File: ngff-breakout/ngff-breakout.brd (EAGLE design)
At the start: 70 x 70 mm, 43 parts, among them K1 694108106102, U1 IP4234CZ6, U2 LD1085D2T33R, X2 MINI-USB-SHIELD-UX60-MB-5ST

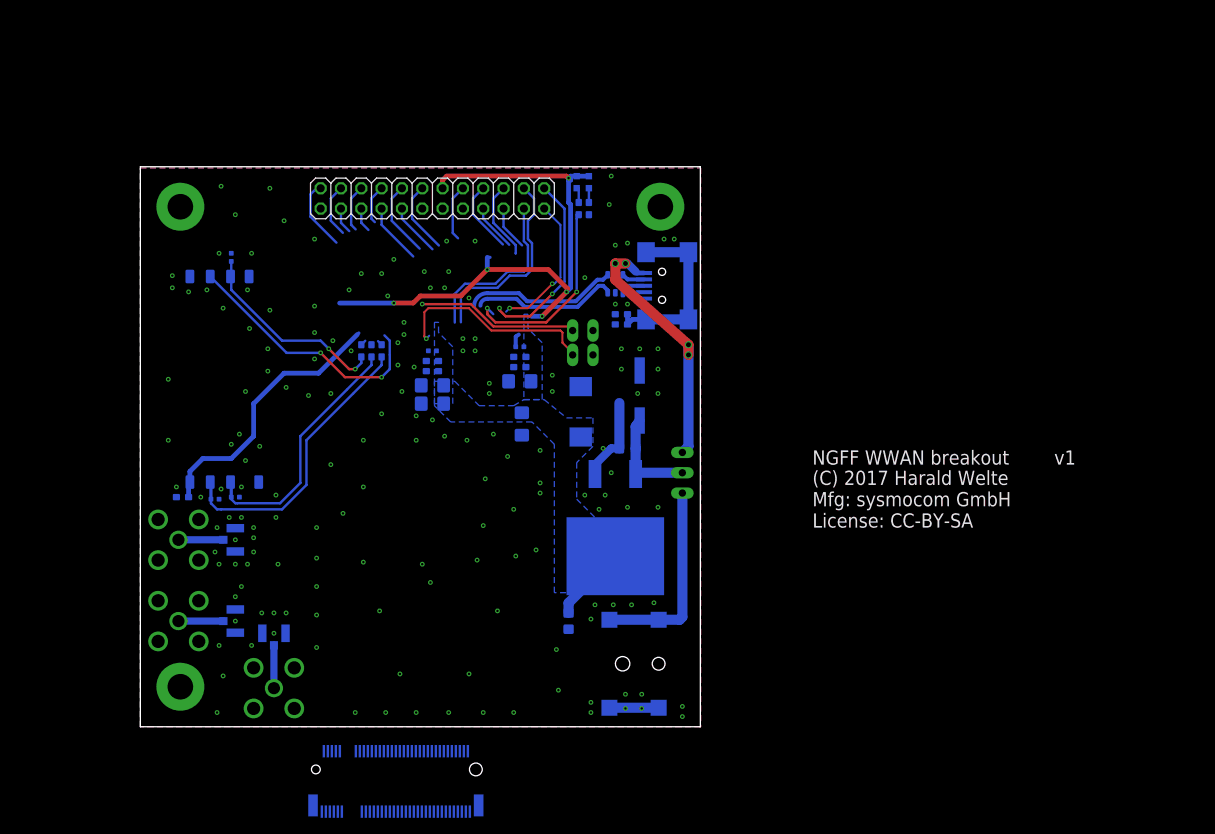
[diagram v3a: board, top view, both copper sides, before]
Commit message: ngff-breakout: intermediate state
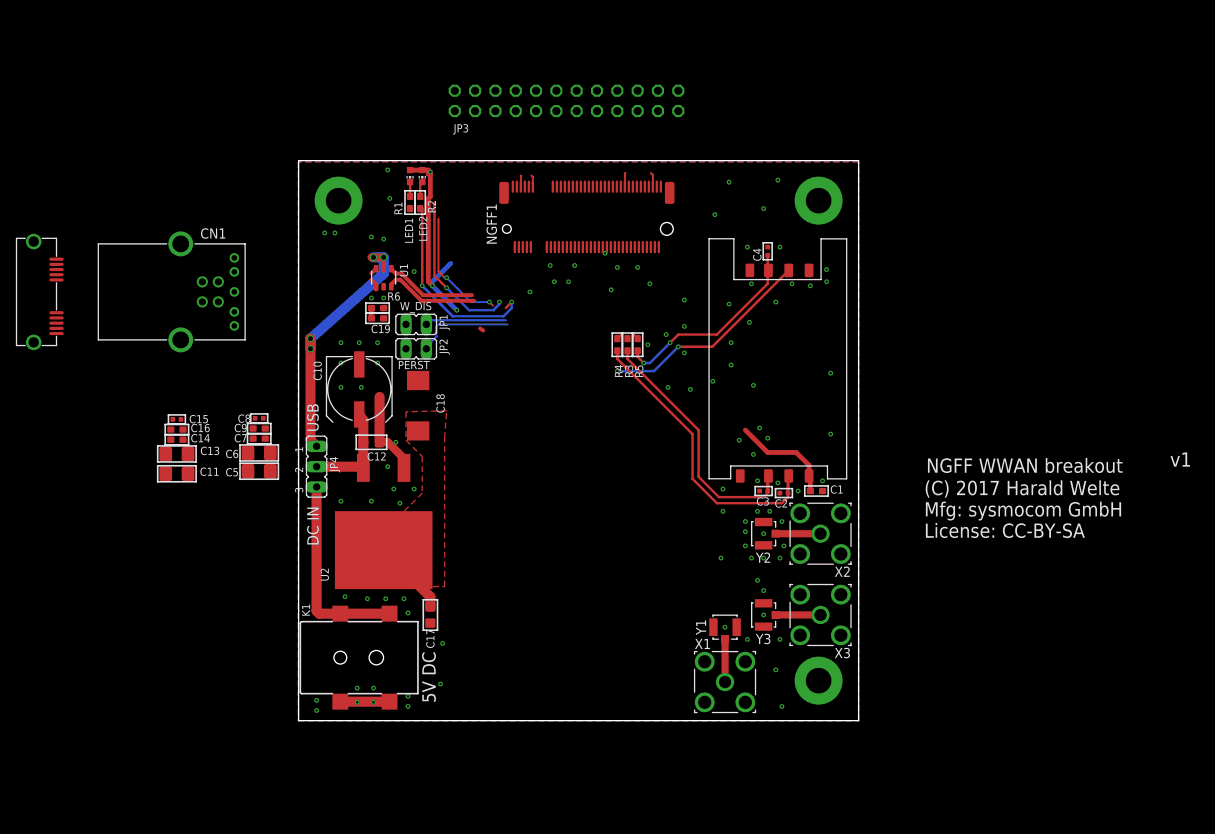
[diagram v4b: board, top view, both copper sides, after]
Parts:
- removed C105, C109: 100u, rc-sysmocom:1206
- removed C106, C110: 100n, rc-sysmocom:_0603
- removed C107, C111: 33p, rc-sysmocom:_0402
- removed C108, C112: 10p, rc-sysmocom:_0603
- removed X4, X5: (no value), laforge:SMA-F-S-TH
- removed Y4, Y5: (no value), laforge:HRS_UFL
- added C12, C17: 10u, rc-sysmocom:_0805
- added C13: 100u, rc-sysmocom:1206
- added C14, C19: 100n, rc-sysmocom:_0603
- added C15: 33p, rc-sysmocom:_0402
- added C16: 10p, rc-sysmocom:_0603
- added C18: DNP, rcl:SMC_E
- added CN1: (no value), USB30B:USB3.0-B
- added CN2: (no value), USB30-MICROB:ZX360D-B
- added X1: (no value), laforge:SMA-F-S-TH
- added Y1, Y2: (no value), laforge:HRS_UFL
- C1: value 10u -> 100n; device rc-sysmocom:_0805 -> rc-sysmocom:_0603
- C10: value 100u -> 470u; device rc-sysmocom:1206 -> rcl:UD-8X10_NICHICON
- C2: value 10u -> 33p; device rc-sysmocom:_0805 -> rc-sysmocom:_0402
- C3: value 470u -> 33p; device rcl:UD-8X10_NICHICON -> rc-sysmocom:_0402
- C4: value DNP -> 33p; device rcl:SMC_E -> rc-sysmocom:_0402
- C5, C6: value 33p -> 100u; device rc-sysmocom:_0402 -> rc-sysmocom:1206
- C7: value 33p -> 100n; device rc-sysmocom:_0402 -> rc-sysmocom:_0603
- C8: value 100n -> 33p; device rc-sysmocom:_0603 -> rc-sysmocom:_0402
- C9: value 100n -> 10p
- JP3: device jumper:JP2 -> pinhead:2X12
- JP4: device pinhead:2X12 -> jumper:JP2
- LED1: value YELLOW -> GREEN
- LED2: value GREEN -> YELLOW
- R1, R2: value 47 -> 330
- R4: value 1M -> 47
- R5: value 330 -> 47
- R6: value 330 -> 1M
- X2: value MINI-USB-SHIELD-UX60-MB-5ST -> (none); device con-hirose:UX60-MB-5ST -> laforge:SMA-F-S-TH
- moved X3 80.8 mm to (65.0, 14.0), flipped to the top
- moved NGFF1 71.7 mm to (35.8, 62.2), flipped to the top, turned to 0 degrees
- moved SIM1 69.6 mm to (59.7, 44.2), flipped to the top
- moved Y3 66.7 mm to (57.9, 14.0), flipped to the top
- moved K1 49.8 mm to (0.00, 8.64), flipped to the top
- moved JP3 48.7 mm to (33.3, 78.2), turned to 0 degrees
- moved C9 47.1 mm to (-5.14, 37.3), flipped to the top, turned to 0 degrees
- moved C11 43.6 mm to (-15.4, 31.6), flipped to the top, turned to 180 degrees
- moved X2 36.8 mm to (65.0, 24.1), flipped to the top, turned to 180 degrees
- moved JP4 36.5 mm to (2.03, 32.5), turned to 270 degrees
- moved C2 31.3 mm to (60.5, 29.2), flipped to the top, turned to 180 degrees
- moved C4 30.8 mm to (58.4, 59.4), flipped to the top
- moved R3 30.7 mm to (40.9, 47.8), flipped to the top
- moved U1 29.0 mm to (10.4, 56.1), flipped to the top
- moved U2 29.0 mm to (10.4, 25.7), flipped to the top
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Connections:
- removed net N$14 (its old number): X4.C, Y4.SIG
- new net N$11: CN1.6
- new net N$13: X2.C, Y2.SIG
- new net N$15: CN1.7
- new net N$17: CN1.8
- new net N$18: CN1.9
- new net N$4: CN1.5
- new net USB3.0_RX_N: NGFF1.35
- new net USB3.0_RX_P: NGFF1.37
- new net USB3.0_TX_N: NGFF1.29
- new net USB3.0_TX_P: NGFF1.31
- net !CLKREQ: now also JP3.6; no longer JP4.6
- net COEX1: now also JP3.4; no longer JP4.4
- net COEX2: now also JP3.3; no longer JP4.3
- net GND: now also C10.-, C12.1, C13.1, C14.1, C15.2, C16.2, C17.1, C18.-, C19.1, C2.2, C3.2, C4.2, C5.1, C6.1, C7.1, C8.2, C9.2, CN1.4, JP1.1, JP2.2, JP3.1, JP3.13, R1.1, R6.1, X1.G1, X1.G2, X1.G3, X1.G4, X2.G1, X2.G2, X2.G3, X2.G4, Y1.GND@1, Y1.GND@2, Y2.GND@1, Y2.GND@2; no longer C10.1, C105.1, C106.1, C107.2, C108.2, C109.1, C110.1, C111.2, C112.2, C2.1, C3.-, C4.-, C5.2, C6.2, C7.2, C8.1, C9.1, JP1.2, JP2.1, JP4.1, JP4.13, R4.1, R5.1, X2.5, X4.G1, X4.G2, X4.G3, X4.G4, X5.G1, X5.G2, X5.G3, X5.G4, Y4.GND@1, Y4.GND@2, Y5.GND@1, Y5.GND@2
- net LDO_IN: now also C10.+, C12.2, JP4.2; no longer C1.2, C3.+, JP3.2
- net LED_WLAN: now also JP3.24; no longer JP4.24
- net LED_WPAN: now also JP3.23; no longer JP4.23
- net N$1: now also LED1.C, R1.2; no longer LED2.C, R5.2
- net N$10: now also C19.2, CN1.S1, CN1.S2, R6.2; no longer C9.2, R4.2, X2.M1, X2.M2, X2.M3, X2.M4
- net N$12: now also JP4.3; no longer JP3.3
- net N$16: now also JP3.11; no longer JP4.11
- net N$2: now also LED2.C, R2.1; no longer LED1.C, R6.1
- net N$3: now also R2.2; no longer R6.2
- net N$5: now also R5.1; no longer R1.1
- net N$7: now also X1.C, Y1.SIG; no longer X5.C, Y5.SIG
- net N$8: now also R3.1; no longer R2.1
- net N$9: now also R4.1; no longer R3.1
- net PERN0: now also JP3.9; no longer JP4.9
- net PERP0: now also JP3.12; no longer JP4.12
- net PERST: now also JP2.1; no longer JP1.1
- net PETN0: now also JP3.16; no longer JP4.16
- net PETP0: now also JP3.15; no longer JP4.15
- net REFCLK+: now also JP3.8; no longer JP4.8
- net REFCLK-: now also JP3.5; no longer JP4.5
- net RSVRD45: now also JP3.18; no longer JP4.18
- net RSVRD47: now also JP3.17; no longer JP4.17
- net RSVRD49: now also JP3.20; no longer JP4.20
- net RSVRD51: now also JP3.19; no longer JP4.19
- net SMB_CLK: now also JP3.21; no longer JP4.21
- net SMB_DATA: now also JP3.22; no longer JP4.22
- net UIM_C4: now also JP3.10; no longer JP4.10
- net UIM_C8: now also JP3.7; no longer JP4.7
- net USB_VBUS: now also CN1.1, JP4.1; no longer JP3.1, X2.1
- net USIM_CLK: now also C3.1, R3.2; no longer C5.1, R2.2
- net USIM_DATA: now also C4.1, R5.2; no longer C7.1, R1.2
- net USIM_POWER: now also C1.2; no longer C8.2
- net USIM_RESET: now also C2.1, R4.2; no longer C6.1, R3.2
- net VCC_3V3: now also C13.2, C14.2, C15.1, C16.1, C17.2, C18.+, C5.2, C6.2, C7.2, C8.1, C9.1, JP3.14; no longer C10.2, C105.2, C106.2, C107.1, C108.1, C109.2, C110.2, C111.1, C112.1, C2.2, C4.+, JP4.14
- net WAKE: now also JP3.2; no longer JP4.2
- net W_DISABLE: now also JP1.2; no longer JP2.2
- net _USB_D_N: now also CN1.2; no longer X2.2
- net _USB_D_P: now also CN1.3; no longer X2.3
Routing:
- net VCC_3V3: track 83.3 -> 35.2 mm, vias 5 -> 3
- net SMB_DATA: track 24.9 -> 0.00 mm
- net SMB_CLK: track 21.7 -> 0.00 mm
- net N$10: track 22.8 -> 1.27 mm
- net USIM_POWER: track 33.9 -> 13.1 mm
- net PERST: track 26.0 -> 12.3 mm, vias 1 -> 0
- net W_DISABLE: track 20.3 -> 10.1 mm, vias 1 -> 0
- net RSVRD49: track 9.83 -> 0.00 mm
- net UIM_C4: track 9.51 -> 0.00 mm
- net RSVRD45: track 9.09 -> 0.00 mm
- net PERP0: track 9.06 -> 0.00 mm
- net WAKE: track 8.96 -> 0.00 mm
- net USB_D_N: track 19.2 -> 11.5 mm
- net UIM_C8: track 7.62 -> 0.00 mm
- net PETN0: track 7.05 -> 0.00 mm
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- added copper zone on layer 1, net VCC_3V3
- removed copper zone on layer 16, net VCC_3V3
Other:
- board text removed: "1"

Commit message: ngff-breakout: almost ready
missing: more vias, more ext. attributes (for BOM)
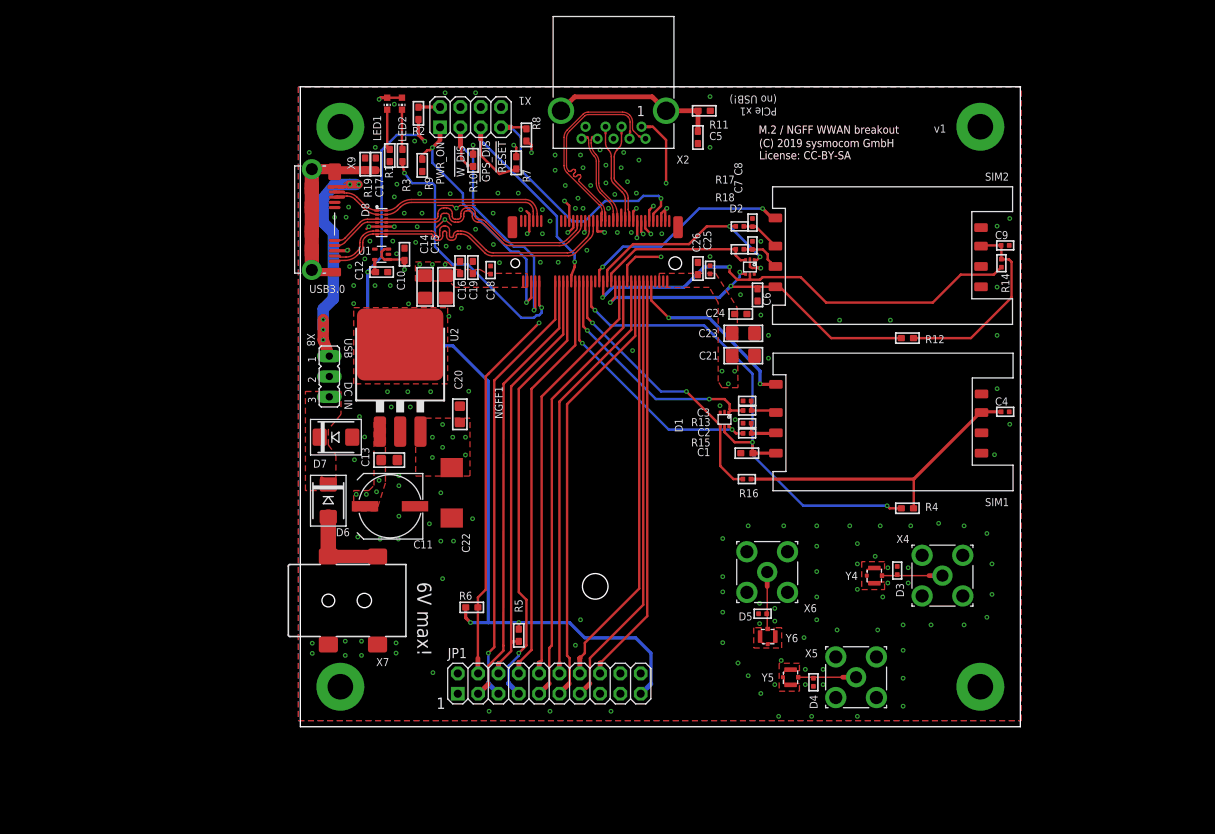
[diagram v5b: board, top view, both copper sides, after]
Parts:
- removed CN1: (no value), USB30B:USB3.0-B
- removed CN2: (no value), USB30-MICROB:ZX360D-B
- removed JP2: (no value), jumper:JP1
- removed JP3: (no value), pinhead:2X12
- removed JP4: (no value), jumper:JP2
- removed K1: 694108106102, Wurth_Elektronik_Electromechanic_DC_Power_Jack_Connectors_rev15c:694108106102
- removed X3: (no value), laforge:SMA-F-S-TH
- removed Y1, Y2, Y3: (no value), laforge:HRS_UFL
- added C20: 10u, rc-sysmocom:_0805
- added C21, C23: 100u, rc-sysmocom:1206
- added C22: DNP, rcl:SMC_E
- added C24: 100n, rc-sysmocom:_0603
- added C25: 33p, rc-sysmocom:_0402
- added C26: 10p, rc-sysmocom:_0603
- added D1, D2: PESD5V0UBV, laforge:SOT666
- added D3, D4, D5: GG040205170N2P, diodes-sysmocom:_0402
- added D6: SD2114S040S5R0, diodes-sysmocom:SMBDIODE
- added D7: SMBJP6KE6.8A-TP, diodes-sysmocom:SMBDIODE
- added D8: SP3012-6UTG, SP3012:UDFN-14
- added R10, R7, R8, R9: 10k, rc-sysmocom:_0603
- added R11, R19: 330, rc-sysmocom:_0603
- added R12: DNP, rc-sysmocom:_0603
- added R13, R14, R15, R16, R17, R18: 47, rc-sysmocom:_0402
- added SIM2: SF7W008S1A-R, SF7W008S1A-SIM:SF7W008S1A-RESTR
- added X4, X5, X6: (no value), laforge:SMA-F-S-TH
- added X7: 694108106102, Wurth_Elektronik_Electromechanic_DC_Power_Jack_Connectors_rev15c:694108106102
- added X8: (no value), jumper:JP2
- added X9: ZX360D-B-10P(30), USB30-MICROB:ZX360D-B
- added Y4, Y5, Y6: MHF4, con-MHF4:MURATA_HSC
- C10: value 470u -> 100n; device rcl:UD-8X10_NICHICON -> rc-sysmocom:_0603
- C11: value 100u -> 470u; device rc-sysmocom:1206 -> rcl:UD-8X10_NICHICON
- C12, C17: value 10u -> 100n; device rc-sysmocom:_0805 -> rc-sysmocom:_0603
- C13: value 100u -> 10u; device rc-sysmocom:1206 -> rc-sysmocom:_0805
- C14: value 100n -> 100u; device rc-sysmocom:_0603 -> rc-sysmocom:1206
- C15: value 33p -> 100u; device rc-sysmocom:_0402 -> rc-sysmocom:1206
- C16: value 10p -> 100n
- C18: value DNP -> 33p; device rcl:SMC_E -> rc-sysmocom:_0402
- C19: value 100n -> 10p
- C5, C6: value 100u -> 100n; device rc-sysmocom:1206 -> rc-sysmocom:_0603
- C7: value 100n -> 33p; device rc-sysmocom:_0603 -> rc-sysmocom:_0402
- C9: value 10p -> 33p; device rc-sysmocom:_0603 -> rc-sysmocom:_0402
- JP1: device jumper:JP1 -> laforge:2X10
- R2: value 330 -> 10k
- R3: value 47 -> 330
- R4: value 47 -> DNP
- R5: value 47 -> 10k
- R6: value 1M -> 10k
- U1: value IP4234CZ6 -> (none); device laforge:TSOP-6 -> ldo:SC70-5
- U2: device ldo:ST_D2PAK -> ldo:TO263
- X1: value (none) -> PINHD-2X4; device laforge:SMA-F-S-TH -> laforge:2X04
- X2: device laforge:SMA-F-S-TH -> InputOutputIO (rev19a):692121030100
- moved C9 96.0 mm to (88.1, 60.2)
- moved X1 77.4 mm to (21.3, 76.2)
- moved C5 68.9 mm to (49.7, 73.7), turned to 90 degrees
- moved C8 66.3 mm to (56.5, 63.0), turned to 90 degrees
- moved C7 66.2 mm to (56.5, 60.2), turned to 90 degrees
- moved C6 65.3 mm to (57.1, 54.0), turned to 90 degrees
- moved C17 56.8 mm to (9.43, 70.3), turned to 270 degrees
- moved X2 55.7 mm to (39.1, 73.5)
- moved JP1 47.9 mm to (31.1, 5.40), turned to 0 degrees
- moved R4 41.6 mm to (75.9, 27.3), turned to 0 degrees
- moved C16 40.8 mm to (20.0, 57.4), turned to 270 degrees
- moved R5 39.2 mm to (27.3, 11.4), turned to 90 degrees
- moved R6 39.2 mm to (21.4, 14.9)
- moved C15 37.5 mm to (18.2, 55.0), turned to 90 degrees
- moved R3 36.8 mm to (12.8, 71.4)
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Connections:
- net USIM_VPP renamed N$8
- removed net LED_WLAN: JP3.24
- removed net LED_WPAN: JP3.23
- removed net N$11: CN1.6
- removed net N$15: CN1.7
- removed net N$16: JP3.11
- removed net N$8 (its old number): NGFF1.32, R3.1
- removed net N$9: NGFF1.30, R4.1
- removed net PERN0: JP3.9
- removed net PERP0: JP3.12
- removed net PERST: JP2.1, NGFF1.67
- removed net PETN0: JP3.16
- removed net PETP0: JP3.15
- removed net REFCLK+: JP3.8
- removed net REFCLK-: JP3.5
- removed net RSVRD45: JP3.18
- removed net RSVRD47: JP3.17
- removed net RSVRD49: JP3.20
- removed net RSVRD51: JP3.19
- removed net UIM_C4: JP3.10
- removed net UIM_C8: JP3.7
- removed net USB_D_N: NGFF1.9, U1.4
- removed net USB_D_P: NGFF1.7, U1.3
- removed net USIM_CLK: C3.1, R3.2, SIM1.3
- removed net USIM_DATA: C4.1, R5.2, SIM1.7
- removed net USIM_POWER: C1.2, NGFF1.36, SIM1.1
- removed net USIM_RESET: C2.1, R4.2, SIM1.2
- removed net WAKE: JP3.2, NGFF1.23
- removed net W_DISABLE: JP1.2, NGFF1.8
- new net !BODY_SAR: JP1.4, NGFF1.25, R6.1
- new net !GPS_DISABLE: NGFF1.26, R7.1, X1.5
- new net !PERST: JP1.10, NGFF1.50
- new net !RESET: NGFF1.67, R8.1, X1.7
- new net !USIM1_RESET: C2.1, R15.2, SIM1.2
- new net !USIM2_RESET: C7.1, R18.2, SIM2.2
- new net !WAKE: NGFF1.54, X2.1
- new net !WAKE_ON_WWAN: JP1.6, NGFF1.23, R5.1
- new net !W_DISABLE: NGFF1.8, R10.1, X1.3
- new net ANTCTL0: JP1.15, NGFF1.59
- new net ANTCTL1: JP1.18, NGFF1.61
- new net ANTCTL2: JP1.17, NGFF1.63
- new net ANTCTL3: JP1.20, NGFF1.65
- new net COEX3: JP1.14, NGFF1.60
- new net N$6: NGFF1.10, R3.2
- new net PCIE_RX_N: NGFF1.47, X2.5
- new net PCIE_RX_P: NGFF1.49, X2.6
- new net PCIE_TX_N: NGFF1.41, X2.9
- new net PCIE_TX_P: NGFF1.43, X2.8
- new net PCM_CLK: JP1.5, NGFF1.20
- new net PCM_DIN: JP1.3, NGFF1.22
- new net PCM_DOUT: JP1.7, NGFF1.24
- new net PCM_SYNC: JP1.8, NGFF1.28
- new net PWR_ON: NGFF1.6, R9.2, X1.1
- new net REFCLK_N: NGFF1.53, X2.3
- new net REFCLK_P: NGFF1.55, X2.2
- new net SIM1_DET: NGFF1.66, SIM1.81
- new net SIM2_DET: NGFF1.40, SIM2.81
- new net USIM1_CLK: C3.1, R13.2, SIM1.3
- new net USIM1_DATA: C4.1, R16.2, R4.2, SIM1.7
- new net USIM1_POWER: C1.2, D1.5, NGFF1.36, R4.1, SIM1.1
- new net USIM2_CLK: C8.1, R17.2, SIM2.3
- new net USIM2_DATA: C9.1, R12.2, R14.2, SIM2.7
- new net USIM2_POWER: C6.2, D2.4, NGFF1.48, R12.1, SIM2.1
- new net VCC_1V8: C12.2, JP1.19, R10.2, R2.2, R5.2, R6.2, R7.2, R8.2, U1.5
- new net _!USIM1_RESET: D1.6, NGFF1.30, R15.1
- new net _!USIM2_RESET: D2.3, NGFF1.46, R18.1
- new net _USIM1_CLK: D1.1, NGFF1.32, R13.1
- new net _USIM1_DATA: D1.4, NGFF1.34, R16.1
- new net _USIM2_CLK: D2.1, NGFF1.44, R17.1
- new net _USIM2_DATA: D2.5, NGFF1.42, R14.1
- net !CLKREQ: now also JP1.9, NGFF1.52; no longer JP3.6
- net COEX1: now also JP1.16; no longer JP3.4
- net COEX2: now also JP1.13; no longer JP3.3
- net GND: now also C10.1, C11.-, C15.1, C16.1, C18.2, C19.2, C20.1, C21.1, C22.-, C23.1, C24.1, C25.2, C26.2, C7.2, D1.2, D2.2, D3.1, D4.1, D5.1, D7.A, D8.10, JP1.2, R11.1, R19.1, R9.1, SIM1.82, SIM2.5, SIM2.82, U2.2, U2.4, X1.4, X1.6, X1.8, X4.G1, X4.G2, X4.G3, X4.G4, X5.G1, X5.G2, X5.G3, X5.G4, X6.G1, X6.G2, X6.G3, X6.G4, X7.2, X7.3, X9.5, X9.8, Y4.P$1, Y4.P$2, Y4.P$4, Y5.P$1, Y5.P$2, Y5.P$4, Y6.P$1, Y6.P$2, Y6.P$4; no longer C10.-, C11.1, C15.2, C16.2, C18.-, C19.1, C7.1, CN1.4, JP1.1, JP2.2, JP3.1, JP3.13, K1.2, K1.3, R6.1, U2.LEFT, X1.G1, X1.G2, X1.G3, X1.G4, X2.G1, X2.G2, X2.G3, X2.G4, X3.G1, X3.G2, X3.G3, X3.G4, Y1.GND@1, Y1.GND@2, Y2.GND@1, Y2.GND@2, Y3.GND@1, Y3.GND@2
- net LDO_IN: now also C11.+, C13.2, U2.1, X8.2; no longer C10.+, C12.2, JP4.2, U2.RIGHT
- net N$10: now also C17.2, R19.2, X9.S1, X9.S2, X9.S3, X9.S4, X9.S5, X9.S6, X9.S7, X9.S8; no longer C19.2, CN1.S1, CN1.S2, R6.2
- net N$12: now also D6.C, D7.C, X8.3; no longer JP4.3, K1.1, K1.1-1
- net N$13: now also D3.2, X4.C, Y4.1; no longer X2.C, Y2.SIG
- net N$14: now also D4.2, X5.C, Y5.1; no longer X3.C, Y3.SIG
- net N$17: now also X9.4; no longer CN1.8
- net N$18: now also R2.1, X1.2; no longer CN1.9
- net N$2: now also R3.1; no longer R2.1
- net N$3: now also D6.A, X7.1, X7.1-1; no longer R2.2
- net N$4: now also C5.2, R11.2, X2.SHELL, X2.SHELL1; no longer CN1.5
- net N$5: now also SIM2.6; no longer NGFF1.34, R5.1
- net N$7: now also D5.2, X6.C, Y6.1; no longer X1.C, Y1.SIG
- net SMB_CLK: now also JP1.11; no longer JP3.21
- net SMB_DATA: now also JP1.12; no longer JP3.22
- net USB3.0_RX_N: now also D8.9, X9.9
- net USB3.0_RX_P: now also D8.8, X9.10
- net USB3.0_TX_N: now also D8.12, X9.6
- net USB3.0_TX_P: now also D8.11, X9.7
- net USB_VBUS: now also X8.1, X9.1; no longer CN1.1, JP4.1, U1.5
- net VCC_3V3: now also C10.2, C15.2, C16.2, C18.1, C19.1, C20.2, C21.2, C22.+, C23.2, C24.2, C25.1, C26.1, JP1.1, U1.1, U1.3, U2.3; no longer C11.2, C13.2, C15.1, C16.1, C17.2, C18.+, C5.2, C6.2, C7.2, C8.1, C9.1, JP3.14, U2.PAD
- net _USB_D_N: now also D8.14, NGFF1.9, X9.2; no longer CN1.2, U1.6
- net _USB_D_P: now also D8.13, NGFF1.7, X9.3; no longer CN1.3, U1.1
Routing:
- net VCC_1V8: track 0.00 -> 134.2 mm, vias 0 -> 7
- net USIM1_POWER: track 0.00 -> 67.3 mm, vias 0 -> 3
- net !BODY_SAR: track 0.00 -> 66.6 mm, vias 0 -> 2
- net ANTCTL3: track 0.00 -> 65.4 mm, vias 0 -> 1
- net ANTCTL0: track 0.00 -> 64.2 mm, vias 0 -> 1
- net ANTCTL2: track 0.00 -> 64.1 mm, vias 0 -> 1
- net ANTCTL1: track 0.00 -> 60.5 mm, vias 0 -> 1
- net _USIM2_DATA: track 0.00 -> 58.5 mm, vias 0 -> 2
- net !CLKREQ: track 0.00 -> 55.9 mm
- net PCM_DOUT: track 0.00 -> 55.9 mm, vias 0 -> 1
- net PCM_DIN: track 0.00 -> 55.8 mm
- net SMB_CLK: track 0.00 -> 55.7 mm
- net PCM_CLK: track 0.00 -> 55.5 mm, vias 0 -> 1
- net COEX2: track 0.00 -> 54.8 mm
- net !WAKE_ON_WWAN: track 0.00 -> 53.4 mm
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- added copper zone on layer 1, net LDO_IN
- added copper zone on layer 1, net N$12
- added copper zone on layer 1, net USB_VBUS
- added copper zone on layer 15, net VCC_3V3
- removed copper zone on layer 15, net N$6
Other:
- board size 70 x 70 mm -> 90 x 80 mm
- board text added: "!GPS_DIS"
- board text added: "!RESET"
- board text added: "!W_DIS"
- board text added: "(C) 2019 sysmocom GmbH License: CC-BY-SA"
- board text added: "1"
- board text added: "6V max!"
- board text added: "M.2 / NGFF WWAN breakout"
- board text added: "PCIe x1 (no USB!)"
- board text added: "PWR_ON"
- board text added: "SIM1"
- board text added: "SIM2"
- board text added: "USB3.0"
- board text removed: "(C) 2017 Harald Welte Mfg: sysmocom GmbH License: CC-BY-SA"
- board text removed: "5V DC"
- board text removed: "NGFF WWAN breakout"
- board text removed: "PERST"
- board text removed: "W_DIS"

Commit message: ngff: finishing work
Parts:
- added FID1, FID2, FID3: (no value), dicons:VISION_REF15
- added JP501, JP502: FIDUCIALUFIDUCIAL, SparkFun:MICRO-FIDUCIAL
- moved C15 0.32 mm to (17.9, 55.0)
- moved C14 0.32 mm to (15.3, 55.0)
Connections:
- net GND: now also NGFF1.P$1
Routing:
- net GND: track 31.2 -> 39.8 mm
